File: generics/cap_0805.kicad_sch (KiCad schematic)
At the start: 3 parts

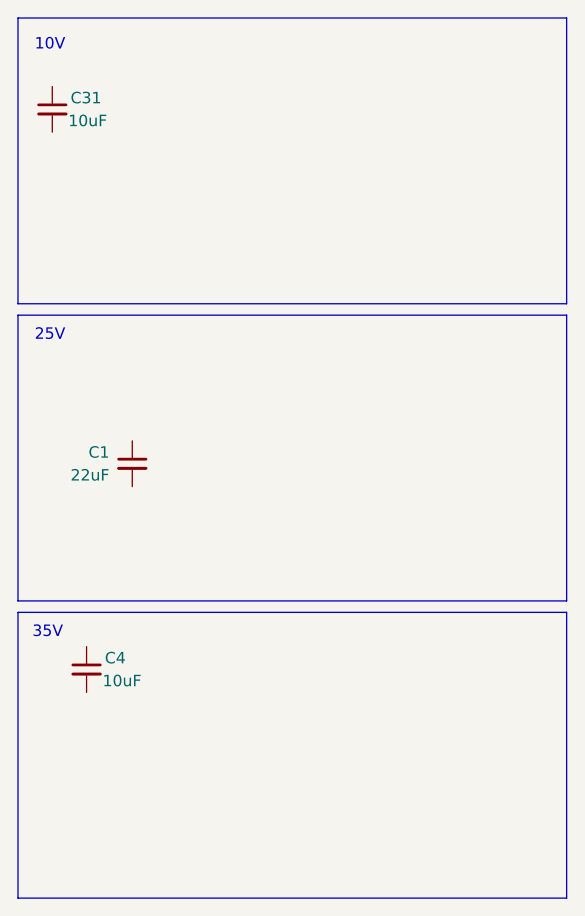
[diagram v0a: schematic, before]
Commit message: - Add Schottky diode and rectifier bridge - Add generics
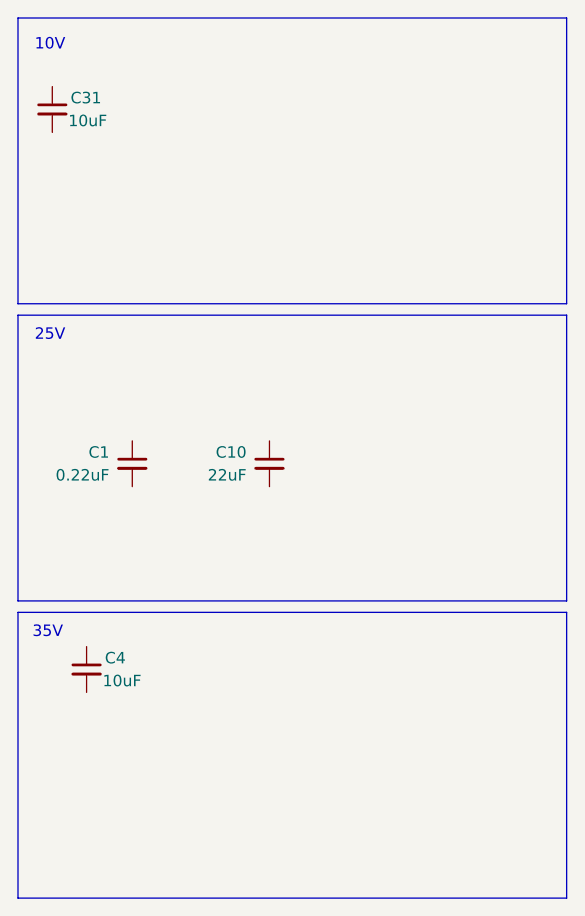
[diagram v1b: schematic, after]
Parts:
- added C10: 22uF, Capacitor_SMD:C_0805_2012Metric, symbol Device:C_Small
- C1: value 22uF -> 0.22uF; Votlage 25V -> (none)
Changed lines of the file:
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@@
+	(symbol
+		(lib_id "Device:C_Small")
+		(at 59.69 69.85 0)
+		(mirror y)
+		(unit 1)
+		(exclude_from_sim no)
+		(in_bom yes)
+		(on_board yes)
+		(dnp no)
+		(fields_autoplaced yes)
+		(property "Reference" "C10"
+			(at 57.15 68.5862 0)
+			(effects
+				(font
+					(size 1.27 1.27)
+				)
+				(justify left)
+			)
+		)
+		(property "Value" "22uF"
+			(at 57.15 71.1262 0)
+			(effects
+				(font
+					(size 1.27 1.27)
+				)
+				(justify left)
+			)
+		)
+		(property "Footprint" "Capacitor_SMD:C_0805_2012Metric"
+			(at 59.69 69.85 0)
+			(effects
+				(font
+					(size 1.27 1.27)
+				)
+				(hide yes)
+			)
+		)
+		(property "Datasheet" "~"
+			(at 59.69 69.85 0)
+			(effects
+				(font
+					(size 1.27 1.27)
+				)
+				(hide yes)
+			)
+		)
+		(property "Description" "Unpolarized capacitor, small symbol"
+			(at 59.69 69.85 0)
+			(effects
+				(font
+					(size 1.27 1.27)
+				)
+				(hide yes)
+			)
+		)
+		(property "MPN" "CL21A226MAQNNNE"
+			(at 59.69 69.85 0)
+			(effects
+				(font
+					(size 1.27 1.27)
+				)
+				(hide yes)
+			)
+		)
+		(property "Mfr" "Samsung"
+			(at 59.69 69.85 0)
+			(effects
+				(font
+					(size 1.27 1.27)
+				)
+				(hide yes)
+			)
+		)
+		(property "Tolerance" "20%"
+			(at 59.69 69.85 0)
+			(effects
+				(font
+					(size 1.27 1.27)
+				)
+				(hide yes)
+			)
+		)
+		(property "LCSC" "C45783"
+			(at 59.69 69.85 0)
+			(effects
+				(font
+					(size 1.27 1.27)
+				)
+				(hide yes)
+			)
+		)
+		(property "Part_Class" "capacitor"
+			(at 59.69 69.85 0)
+			(effects
+				(font
+					(size 1.27 1.27)
+				)
+				(hide yes)
+			)
+		)
+		(pin "2"
+		)
+		(pin "1"
+		)
+		(instances
+			(project "generics"
+				(path "/ff075d90-2677-48ca-91fd-a3a441ca4e63/fc8a1445-9d1d-43d6-bed8-e630a9984c40"
+					(reference "C10")
+					(unit 1)
+				)
+			)
+		)
+	)
 	(symbol
 		(lib_id "Device:C_Small")
@@
 			)
 		)
-		(property "Value" "22uF"
+		(property "Value" "0.22uF"
 			(at 41.91 71.1262 0)
 			(effects
@@
 			(at 44.45 69.85 0)
 			(effects
-				(font
-					(size 1.27 1.27)
-				)
-				(hide yes)
-			)
-		)
-		(property "Votlage" "25V"
-			(at 44.45 69.85 0)
-			(effects
